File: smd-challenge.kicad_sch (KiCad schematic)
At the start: 20 parts, among them J1 DX07S016JA1R1500, U1 ATmega16U2-M, Y1 J49SMH-A-G-G-K-16M0

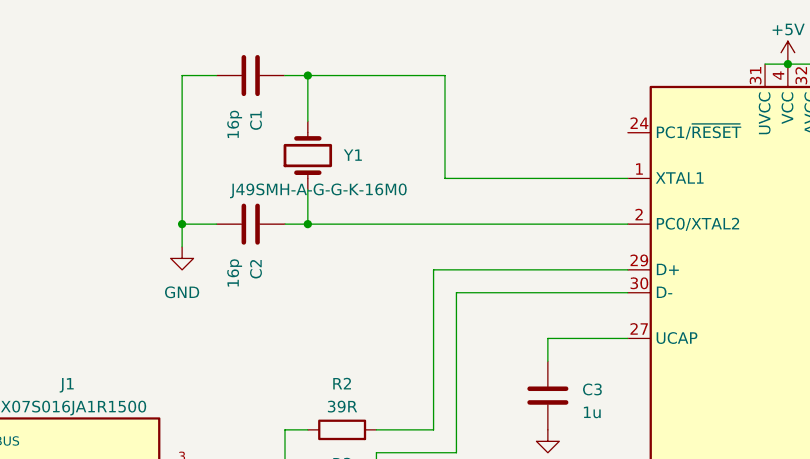
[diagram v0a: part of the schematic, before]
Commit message: Swap crystal for something smaller; settle on layout
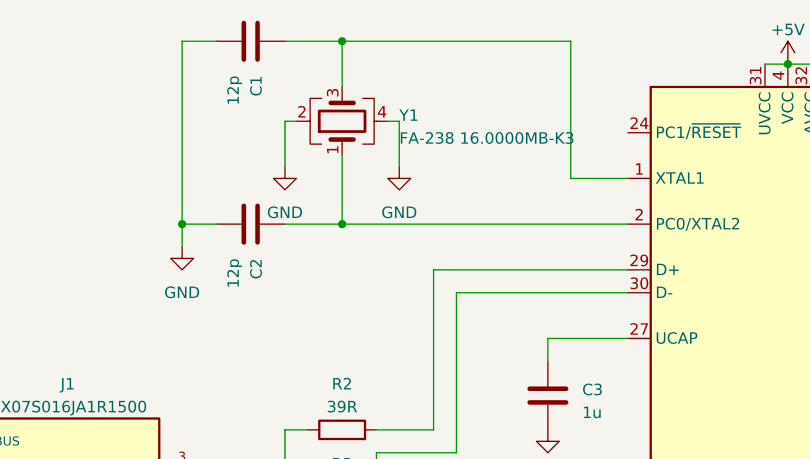
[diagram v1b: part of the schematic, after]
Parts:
- removed Y1: J49SMH-A-G-G-K-16M0, Crystal:Crystal_SMD_SeikoEpson_MC405-2Pin_9.6x4.1mm, symbol Device:Crystal
- added Y1: FA-238 16.0000MB-K3, Crystal:Crystal_SMD_SeikoEpson_FA238-4Pin_3.2x2.5mm, symbol Device:Crystal_GND24
- C1, C2: value 16p -> 12p
- J1: footprint JAE_DX07S016JA1R1500 -> USBConn6:JAE_DX07S016JA1R1500
- U1: footprint Package_DFN_QFN:QFN-32-1EP_5x5mm_P0.5mm_EP3.1x3.1mm -> Package_DFN_QFN:QFN-32-1EP_5x5mm_P0.5mm_EP3.3x3.3mm_ThermalVias
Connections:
- net GND: now also Y1.2, Y1.4
- net at C2.1, U1.2 (PC0/XTAL2): now also Y1.1
- net at C1.1, U1.1 (XTAL1): now also Y1.3
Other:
- moved on the sheet: C1

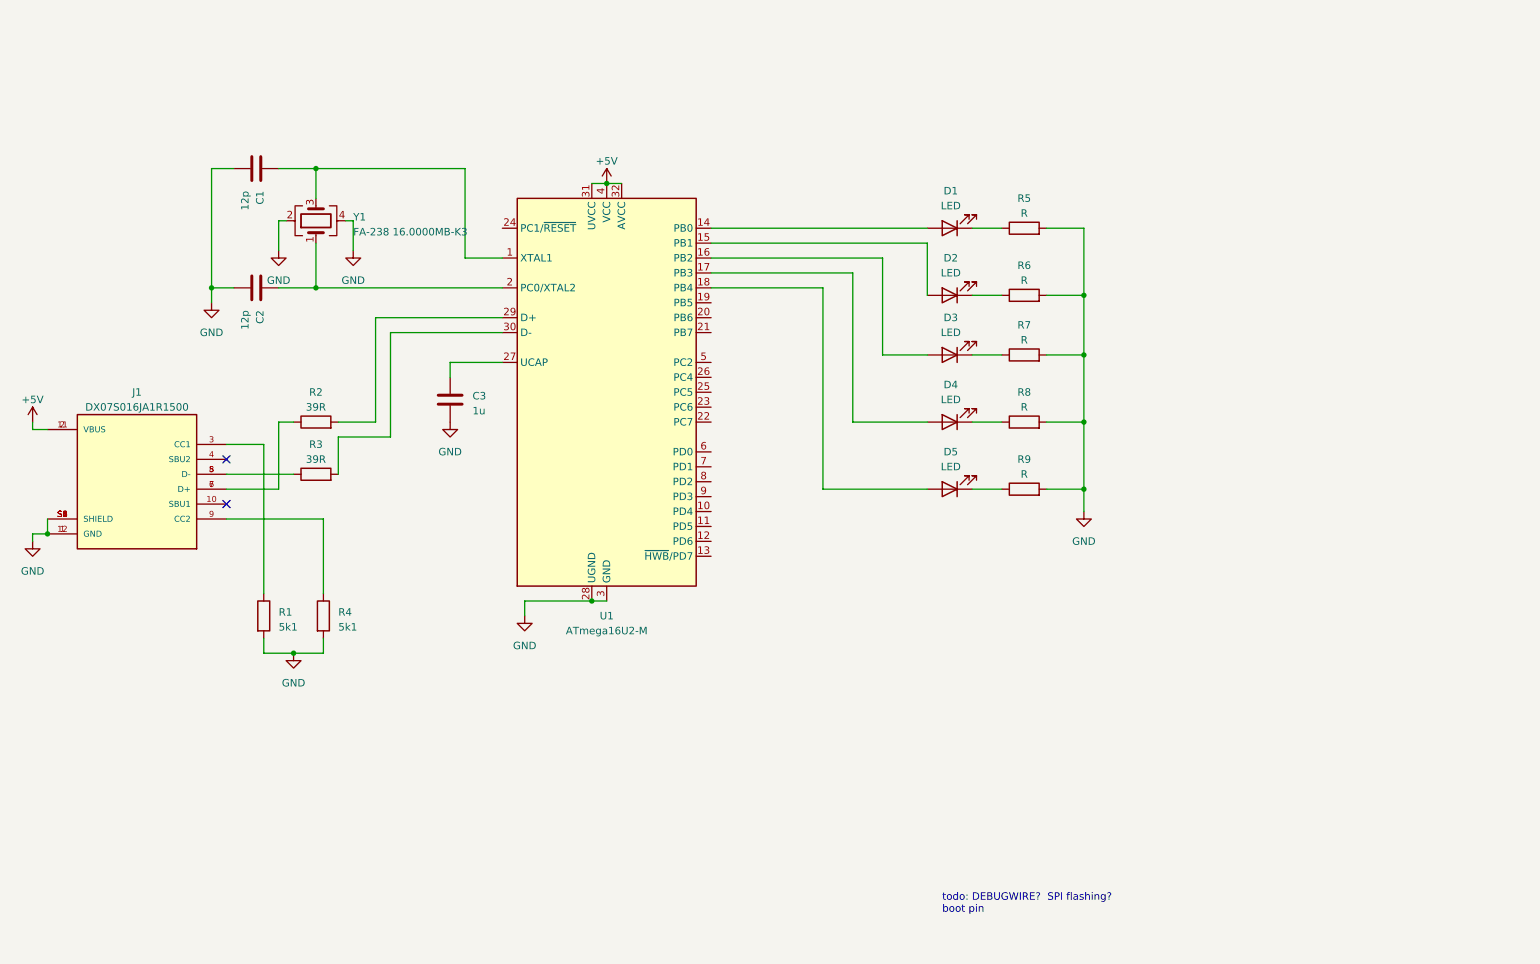
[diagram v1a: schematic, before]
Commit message: Layout with the SAMD21.
The only thing I really don't like is the snakey 3.3V rail but since I
can stitch the grounds back together via the B.Cu zone, it's mostly
fine.
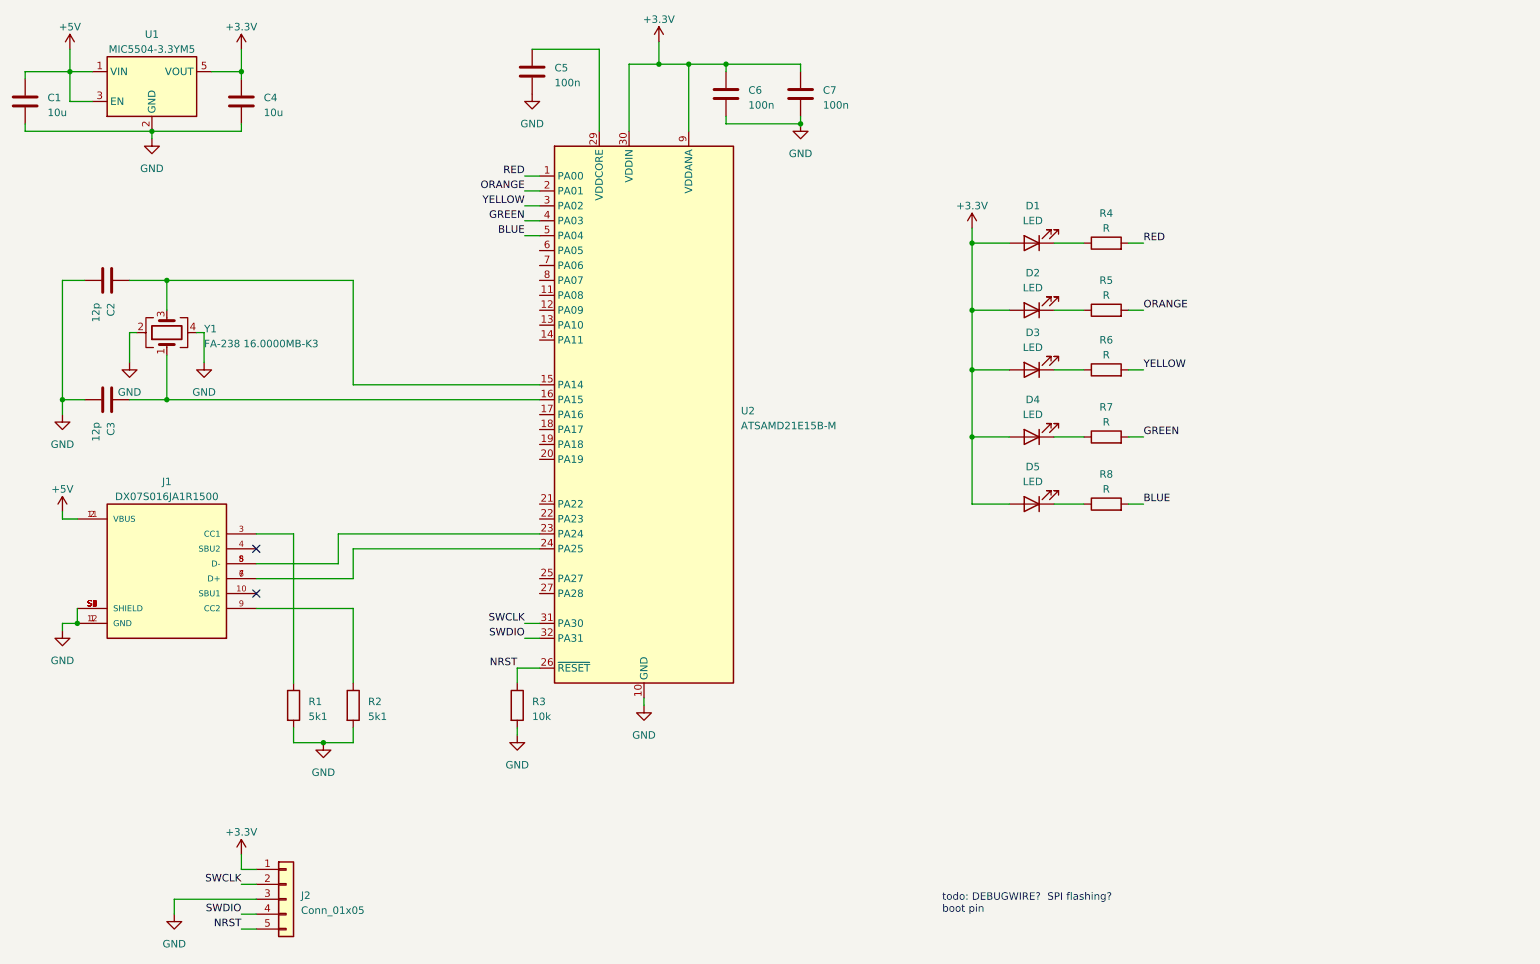
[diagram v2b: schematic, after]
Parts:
- removed C3: 1u, Capacitor_SMD:C_0805_2012Metric, symbol Device:C
- removed R2: 39R, Resistor_SMD:R_0603_1608Metric, symbol Device:R
- removed U1: ATmega16U2-M, Package_DFN_QFN:QFN-32-1EP_5x5mm_P0.5mm_EP3.3x3.3mm_ThermalVias, symbol MCU_Microchip_ATmega:ATmega16U2-M
- added C1, C4: 10u, Capacitor_SMD:C_1206_3216Metric, symbol Device:C
- added C5, C6, C7: 100n, Capacitor_SMD:C_0603_1608Metric, symbol Device:C
- added J2: Conn_01x05, Connector_PinHeader_2.54mm:PinHeader_1x05_P2.54mm_Vertical, symbol Connector_Generic:Conn_01x05
- added U1: MIC5504-3.3YM5, Package_TO_SOT_SMD:SOT-23-5, symbol Regulator_Linear:MIC5504-3.3YM5
- added U2: ATSAMD21E15B-M, Package_DFN_QFN:QFN-32-1EP_5x5mm_P0.5mm_EP3.6x3.6mm, symbol MCU_Microchip_SAMD:ATSAMD21E15B-M
- R3: value 39R -> 10k
- renumbered C1 to C2, C2 to C3, R4 to R2, R5 to R4, R6 to R5, R7 to R6, R8 to R7, R9 to R8
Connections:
- net +5V: now also C1.1, U1.1 (VIN), U1.3 (EN)
- net GND: now also R3.2, C1.2, C4.2, C5.2, C6.2, C7.2, J2.3 (Pin_3), U1.2 (GND), U2.10 (GND), U2.28 (GND); no longer R4.2, R5.2, R6.2, R7.2, R8.2
- net +3V3: now reaches D4.2 (A)
- net +3V3: now also D1.2 (A), D2.2 (A), D3.2 (A), D5.2 (A), C4.1, C6.1, C7.1, J2.1 (Pin_1), U1.5 (VOUT), U2.30 (VDDIN), U2.9 (VDDANA)
- net at J1.5 (D-), J1.8 (D-): now also U2.23 (PA24); no longer R3.1
- net at J1.6 (D+), J1.7 (D+): now also U2.24 (PA25)
- net at C2.1, Y1.3: now also U2.15 (PA14)
- net at C3.1, Y1.1: now also U2.16 (PA15)
- new net: C5.1, U2.29 (VDDCORE)
- new net BLUE: R8.2, U2.5 (PA04)
- new net GREEN: R7.2, U2.4 (PA03)
- new net NRST: J2.5 (Pin_5), R3.1, U2.26 (~RESET)
- new net ORANGE: R5.2, U2.2 (PA01)
- new net RED: R4.2, U2.1 (PA00)
- new net SWCLK: J2.2 (Pin_2), U2.31 (PA30)
- new net SWDIO: J2.4 (Pin_4), U2.32 (PA31)
- new net YELLOW: R6.2, U2.3 (PA02)
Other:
- moved on the sheet: C2, C3, D1, D2, D3, D4, D5, J1, R1, R2, R4, R5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

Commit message: Pick parts for LEDs, values for resistors
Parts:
- D1: Digikey (none) -> 732-4991-1-ND
- D2: Digikey (none) -> 350-4355-1-ND
- D3: Digikey (none) -> 350-2032-1-ND
- D4: Digikey (none) -> 732-11992-1-ND
- D5: Digikey (none) -> 754-2022-1-ND
- R4, R6: value R -> 260
- R5: value R -> 240
- R7: value R -> 130
- R8: value R -> 80
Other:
- note added: "140mcd @ 20mA"
- note added: "150mcd @ 20mA"
- note added: "23.75mcd @ 5mA"
- note added: "25mcd @ 10mA"
- note added: "25mcd @ 5mA"
- note added: "35mcd @ 5mA"
- note added: "37.5mcd @ 5mA"
- note added: "50mcd @ 20mA"
- note added: "95mcd @ 20mA"
- note added: "Vf = 2.0V"
- note added: "Vf = 2.1V"
- note added: "Vf = 2.9V"
- note removed: "todo: DEBUGWIRE? SPI flashing? boot pin"
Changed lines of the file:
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@@
     (stroke (width 0) (type solid) (color 0 0 0 0))
   )
-  (text "todo: DEBUGWIRE?  SPI flashing?\nboot pin" (at 179.07 172.72 0)
-    (effects (font (size 1.27 1.27)) (justify left bottom))
+  (text "Vf = 2.0V" (at 236.22 58.928 180)
+    (effects (font (size 1.27 1.27)) (justify right bottom))
+  )
+  (text "Vf = 2.1V" (at 236.22 69.723 180)
+    (effects (font (size 1.27 1.27)) (justify right bottom))
+  )
+  (text "Vf = 2.0V" (at 236.22 80.01 180)
+    (effects (font (size 1.27 1.27)) (justify right bottom))
+  )
+  (text "Vf = 2.0V" (at 236.22 91.44 180)
+    (effects (font (size 1.27 1.27)) (justify right bottom))
+  )
+  (text "Vf = 2.9V" (at 236.22 102.87 180)
+    (effects (font (size 1.27 1.27)) (justify right bottom))
+  )
+  (text "25mcd @ 5mA" (at 252.73 102.87 180)
+    (effects (font (size 1.27 1.27)) (justify right bottom))
+  )
+  (text "95mcd @ 20mA" (at 254 69.723 180)
+    (effects (font (size 1.27 1.27)) (justify right bottom))
+  )
+  (text "50mcd @ 20mA" (at 254 91.44 180)
+    (effects (font (size 1.27 1.27)) (justify right bottom))
+  )
+  (text "150mcd @ 20mA" (at 255.016 58.928 180)
+    (effects (font (size 1.27 1.27)) (justify right bottom))
+  )
+  (text "140mcd @ 20mA" (at 255.27 80.01 180)
+    (effects (font (size 1.27 1.27)) (justify right bottom))
+  )
+  (text "35mcd @ 5mA" (at 275.844 80.01 180)
+    (effects (font (size 1.27 1.27)) (justify right bottom))
+  )
+  (text "25mcd @ 10mA" (at 277.114 91.44 180)
+    (effects (font (size 1.27 1.27)) (justify right bottom))
+  )
+  (text "37.5mcd @ 5mA" (at 277.876 58.928 180)
+    (effects (font (size 1.27 1.27)) (justify right bottom))
+  )
+  (text "23.75mcd @ 5mA" (at 278.892 69.596 180)
+    (effects (font (size 1.27 1.27)) (justify right bottom))
   )
   (label "SWCLK" (at 59.69 167.64 180)
@@
     (in_bom yes) (on_board yes)
     (property "Reference" "R4" (id 0) (at 207.01 53.34 90))
-    (property "Value" "R" (id 1) (at 207.01 55.88 90))
+    (property "Value" "260" (id 1) (at 207.01 55.88 90))
     (property "Footprint" "Resistor_SMD:R_1206_3216Metric" (id 2) (at 207.01 60.198 90)
       (effects (font (size 1.27 1.27)) hide)
@@
     (in_bom yes) (on_board yes)
     (property "Reference" "R5" (id 0) (at 207.01 64.77 90))
-    (property "Value" "R" (id 1) (at 207.01 67.31 90))
+    (property "Value" "240" (id 1) (at 207.01 67.31 90))
     (property "Footprint" "Resistor_SMD:R_0805_2012Metric" (id 2) (at 207.01 71.628 90)
       (effects (font (size 1.27 1.27)) hide)
@@
     (in_bom yes) (on_board yes)
     (property "Reference" "R6" (id 0) (at 207.01 74.93 90))
-    (property "Value" "R" (id 1) (at 207.01 77.47 90))
+    (property "Value" "260" (id 1) (at 207.01 77.47 90))
     (property "Footprint" "Resistor_SMD:R_0603_1608Metric" (id 2) (at 207.01 81.788 90)
       (effects (font (size 1.27 1.27)) hide)
@@
     (in_bom yes) (on_board yes)
     (property "Reference" "R7" (id 0) (at 207.01 86.36 90))
-    (property "Value" "R" (id 1) (at 207.01 88.9 90))
+    (property "Value" "130" (id 1) (at 207.01 88.9 90))
     (property "Footprint" "Resistor_SMD:R_0402_1005Metric" (id 2) (at 207.01 93.218 90)
       (effects (font (size 1.27 1.27)) hide)
@@
     (in_bom yes) (on_board yes)
     (property "Reference" "R8" (id 0) (at 207.01 97.79 90))
-    (property "Value" "R" (id 1) (at 207.01 100.33 90))
+    (property "Value" "80" (id 1) (at 207.01 100.33 90))
     (property "Footprint" "Resistor_SMD:R_0201_0603Metric" (id 2) (at 207.01 104.648 90)
       (effects (font (size 1.27 1.27)) hide)
@@
       (effects (font (size 1.27 1.27)) hide)
     )
+    (property "Digikey" "732-4991-1-ND" (id 4) (at 194.31 58.42 0)
+      (effects (font (size 1.27 1.27)) hide)
+    )
     (pin "1")
     (pin "2")
@@
       (effects (font (size 1.27 1.27)) hide)
     )
+    (property "Digikey" "350-4355-1-ND" (id 4) (at 194.31 69.85 0)
+      (effects (font (size 1.27 1.27)) hide)
+    )
     (pin "1")
     (pin "2")
@@
       (effects (font (size 1.27 1.27)) hide)
     )
+    (property "Digikey" "350-2032-1-ND" (id 4) (at 194.31 80.01 0)
+      (effects (font (size 1.27 1.27)) hide)
+    )
     (pin "1")
     (pin "2")
@@
       (effects (font (size 1.27 1.27)) hide)
     )
+    (property "Digikey" "732-11992-1-ND" (id 4) (at 194.31 91.44 0)
+      (effects (font (size 1.27 1.27)) hide)
+    )
     (pin "1")
     (pin "2")
@@
     )
     (property "Datasheet" "~" (id 3) (at 194.31 102.87 0)
+      (effects (font (size 1.27 1.27)) hide)
+    )
+    (property "Digikey" "754-2022-1-ND" (id 4) (at 194.31 102.87 0)
       (effects (font (size 1.27 1.27)) hide)
     )
@@
     )
     (path "/1747ca5a-9e5a-4c01-b93a-7a410fe593a0"
-      (reference "R4") (unit 1) (value "R") (footprint "Resistor_SMD:R_1206_3216Metric")
+      (reference "R4") (unit 1) (value "260") (footprint "Resistor_SMD:R_1206_3216Metric")
     )
     (path "/5ed0af24-02c7-4af2-89cc-d5bb665169da"
-      (reference "R5") (unit 1) (value "R") (footprint "Resistor_SMD:R_0805_2012Metric")
+      (reference "R5") (unit 1) (value "240") (footprint "Resistor_SMD:R_0805_2012Metric")
     )
     (path "/789b4679-0534-44b6-b7ca-a241c319e88d"
-      (reference "R6") (unit 1) (value "R") (footprint "Resistor_SMD:R_0603_1608Metric")
+      (reference "R6") (unit 1) (value "260") (footprint "Resistor_SMD:R_0603_1608Metric")
     )
     (path "/66249d1b-1459-4500-9243-7cf52819a6e7"
-      (reference "R7") (unit 1) (value "R") (footprint "Resistor_SMD:R_0402_1005Metric")
+      (reference "R7") (unit 1) (value "130") (footprint "Resistor_SMD:R_0402_1005Metric")
     )
     (path "/be8965f0-4d6b-4950-aaf5-bf69329f5c10"
-      (reference "R8") (unit 1) (value "R") (footprint "Resistor_SMD:R_0201_0603Metric")
+      (reference "R8") (unit 1) (value "80") (footprint "Resistor_SMD:R_0201_0603Metric")
     )
     (path "/5a44c263-eb6c-4a3d-9ffe-d3f0be38b7e7"

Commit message: Pick Digikey part numbers for more things
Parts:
- C2, C3: Digikey (none) -> 1276-1254-1-ND
- R4: Digikey (none) -> RMCF1206JT270RCT-ND
- R5: Digikey (none) -> RMCF0805JT240RCT-ND
- R6: Digikey (none) -> ‎RMCF0603JT270RCT-ND‎
- R7: Digikey (none) -> RMCF0402JT130RCT-ND
- R8: Digikey (none) -> P80.6ABCT-ND
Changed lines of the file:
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@@
   (symbol (lib_id "power:+3.3V") (at 59.69 25.4 0) (unit 1)
     (in_bom yes) (on_board yes)
-    (property "Reference" "#PWR?" (id 0) (at 59.69 29.21 0)
+    (property "Reference" "#PWR0101" (id 0) (at 59.69 29.21 0)
       (effects (font (size 1.27 1.27)) hide)
     )
@@
       (effects (font (size 1.27 1.27)) hide)
     )
+    (property "Digikey" "RMCF1206JT270RCT-ND" (id 4) (at 207.01 58.42 90)
+      (effects (font (size 1.27 1.27)) hide)
+    )
     (pin "1")
     (pin "2")
@@
       (effects (font (size 1.27 1.27)) hide)
     )
+    (property "Digikey" "RMCF0805JT240RCT-ND" (id 4) (at 207.01 69.85 90)
+      (effects (font (size 1.27 1.27)) hide)
+    )
     (pin "1")
     (pin "2")
@@
       (effects (font (size 1.27 1.27)) hide)
     )
+    (property "Digikey" " ‎RMCF0603JT270RCT-ND‎ " (id 4) (at 207.01 80.01 90)
+      (effects (font (size 1.27 1.27)) hide)
+    )
     (pin "1")
     (pin "2")
@@
       (effects (font (size 1.27 1.27)) hide)
     )
+    (property "Digikey" "RMCF0402JT130RCT-ND" (id 4) (at 207.01 91.44 90)
+      (effects (font (size 1.27 1.27)) hide)
+    )
     (pin "1")
     (pin "2")
@@
       (effects (font (size 1.27 1.27)) hide)
     )
+    (property "Digikey" "P80.6ABCT-ND" (id 4) (at 207.01 102.87 90)
+      (effects (font (size 1.27 1.27)) hide)
+    )
     (pin "1")
     (pin "2")
@@
       (effects (font (size 1.27 1.27)) hide)
     )
+    (property "Digikey" "1276-1254-1-ND" (id 4) (at 36.83 64.77 0)
+      (effects (font (size 1.27 1.27)) hide)
+    )
     (pin "1")
     (pin "2")
@@
     )
     (property "Datasheet" "~" (id 3) (at 36.83 85.09 0)
+      (effects (font (size 1.27 1.27)) hide)
+    )
+    (property "Digikey" "1276-1254-1-ND" (id 4) (at 36.83 85.09 0)
       (effects (font (size 1.27 1.27)) hide)
     )
@@
     )
     (path "/2d803b51-daeb-438d-ad31-0a88526c910b"
-      (reference "#PWR?") (unit 1) (value "+3.3V") (footprint "")
+      (reference "#PWR0101") (unit 1) (value "+3.3V") (footprint "")
     )
     (path "/c5fa86be-8e49-41ac-91b5-adef14ae477a"
@@
       (reference "C2") (unit 1) (value "12p") (footprint "Capacitor_SMD:C_0603_1608Metric")
     )
-    (path "/cd860152-eac0-49ea-879a-fe7ad9b85762"
+    (path "/8b358330-234f-4b1c-9989-6037fd57d4c0"
       (reference "C3") (unit 1) (value "12p") (footprint "Capacitor_SMD:C_0603_1608Metric")
     )

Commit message: PCB: swap through-hole for SMD header
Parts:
- J2: footprint Connector_PinHeader_2.54mm:PinHeader_1x05_P2.54mm_Vertical -> Connector_PinHeader_2.54mm:PinHeader_1x05_P2.54mm_Vertical_SMD_Pin1Left
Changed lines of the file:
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@@
       (effects (font (size 1.27 1.27)) (justify left))
     )
-    (property "Footprint" "Connector_PinHeader_2.54mm:PinHeader_1x05_P2.54mm_Vertical" (id 2) (at 67.31 170.18 0)
+    (property "Footprint" "Connector_PinHeader_2.54mm:PinHeader_1x05_P2.54mm_Vertical_SMD_Pin1Left" (id 2) (at 67.31 170.18 0)
       (effects (font (size 1.27 1.27)) hide)
     )
@@
     )
     (path "/bb6c1a15-07b2-4907-aec4-0864d7813a85"
-      (reference "J2") (unit 1) (value "Conn_01x05") (footprint "Connector_PinHeader_2.54mm:PinHeader_1x05_P2.54mm_Vertical")
+      (reference "J2") (unit 1) (value "Conn_01x05") (footprint "Connector_PinHeader_2.54mm:PinHeader_1x05_P2.54mm_Vertical_SMD_Pin1Left")
     )
     (path "/c0814883-8958-4293-ade7-6a478ac7443e"
